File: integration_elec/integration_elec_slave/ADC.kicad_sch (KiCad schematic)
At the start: 1 part, among them U5 ADS1015IDGS

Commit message: EM - fuck it we merge et on cree deux branches
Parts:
- added R21: 2.2k, symbol Device:R_US
- added R22: 22k, Resistor_SMD:R_0805_2012Metric_Pad1.20x1.40mm_HandSolder, symbol Device:R_US
- added R23: 10k, Resistor_SMD:R_0805_2012Metric_Pad1.20x1.40mm_HandSolder, symbol Device:R_US
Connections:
- net +3V3: now also R21.1
- net GND: now also U5.1 (ADDR), R23.2
- net VO_LTF6800: now also R22.1; no longer U5.4 (AIN0)
- net I2C_SCL: now reaches U5.10 (SCL)
- net INT_ADC_OD: now reaches U5.2 (ALERT/RDY)
- net INT_ADC_OD: now also R21.2
- net I2C_SDA: now reaches U5.9 (SDA)
- new net: R22.2, R23.1, U5.4 (AIN0)
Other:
- note added: "0-10V"
- note added: "0-3V"

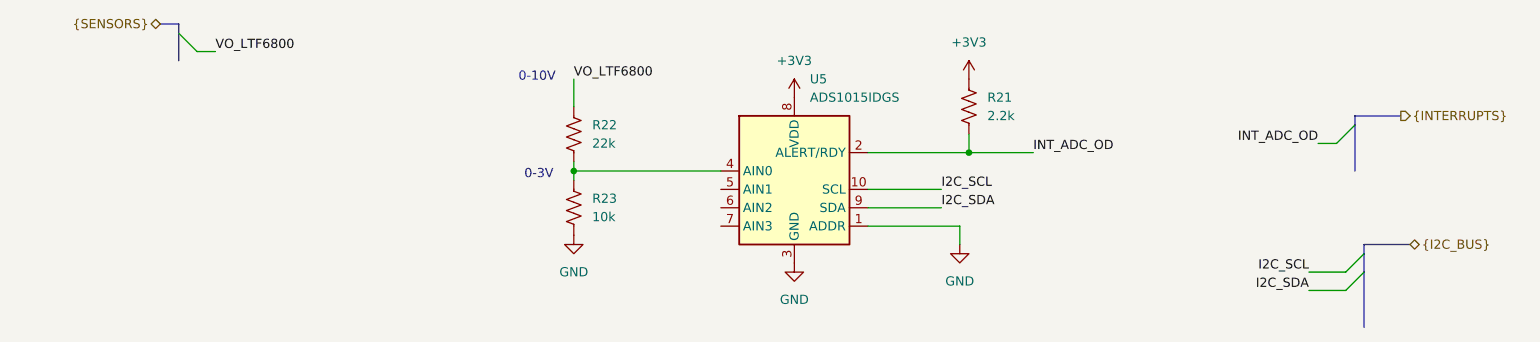
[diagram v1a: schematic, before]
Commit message: EM - Correction des bus
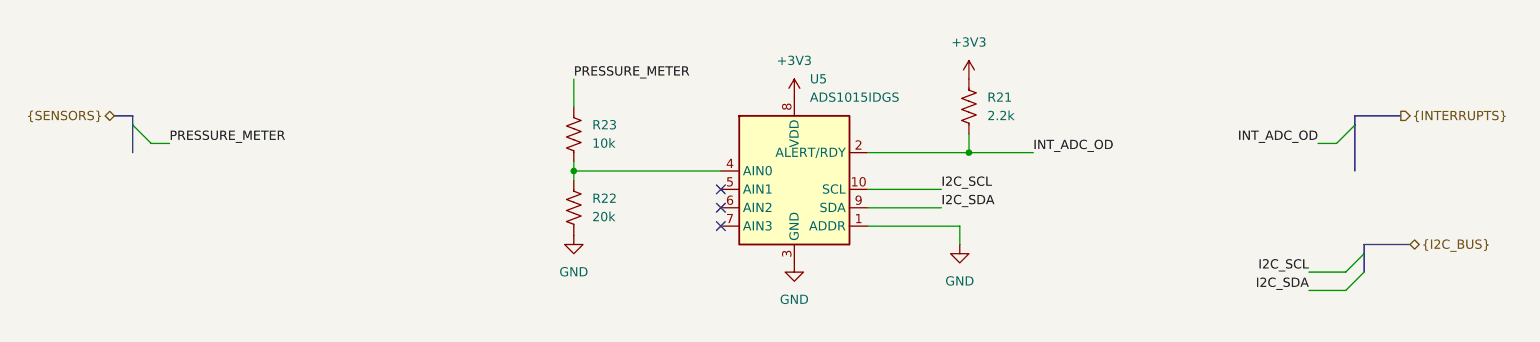
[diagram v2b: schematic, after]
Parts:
- R22: value 22k -> 20k; footprint Resistor_SMD:R_0805_2012Metric_Pad1.20x1.40mm_HandSolder -> (none)
- R23: footprint Resistor_SMD:R_0805_2012Metric_Pad1.20x1.40mm_HandSolder -> (none)
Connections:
- net GND: now also R22.2; no longer R23.2
- net VO_LTF6800: no longer names the net of R22.1
- net VO_LTF6800: now also R23.2, U5.4 (AIN0)
- new net PRESSURE_METER: R23.1
- no-connect marks 0 -> 3
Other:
- note removed: "0-10V"
- note removed: "0-3V"

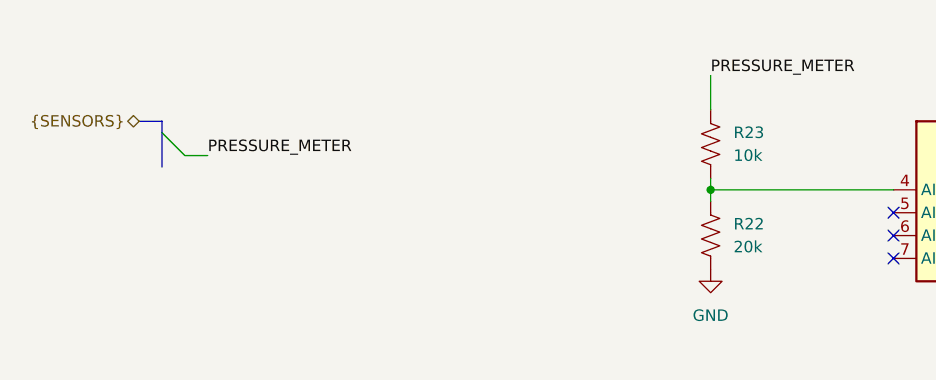
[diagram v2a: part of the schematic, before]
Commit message: EM - Fini schématique attente de review
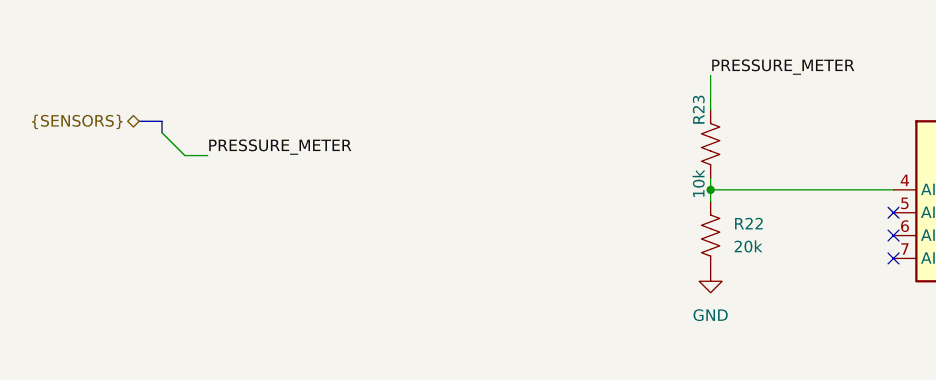
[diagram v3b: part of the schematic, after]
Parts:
- R21: footprint (none) -> Resistor_SMD:R_0805_2012Metric_Pad1.20x1.40mm_HandSolder; DigiKey (none) -> 311-2.20KCRCT-ND
- R22: footprint (none) -> Resistor_SMD:R_0805_2012Metric_Pad1.20x1.40mm_HandSolder; DigiKey (none) -> P20KDACT-ND
- R23: footprint (none) -> Resistor_SMD:R_0805_2012Metric_Pad1.20x1.40mm_HandSolder; DigiKey (none) -> 311-10.0KCRCT-ND; Manufacturer (none) -> Yageo; Manufacturer Part Number (none) -> RC0805FR-0710KL
- U5: DigiKey (none) -> 595-ADS1015IDGSR
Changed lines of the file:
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@@
-		)
-	)
-	(bus
-		(pts
-			(xy 62.23 85.09) (xy 62.23 88.9)
-		)
-		(stroke
-			(width 0)
-			(type default)
 		)
 	)
@@
 			)
 		)
-		(property "Footprint" ""
+		(property "Footprint" "Resistor_SMD:R_0805_2012Metric_Pad1.20x1.40mm_HandSolder"
 			(at 124.206 96.774 90)
 			(effects
@@
 		)
 		(property "Description" "Resistor, US symbol"
+			(at 123.19 96.52 0)
+			(effects
+				(font
+					(size 1.27 1.27)
+				)
+				(hide yes)
+			)
+		)
+		(property "DigiKey" "P20KDACT-ND"
 			(at 123.19 96.52 0)
 			(effects
@@
 				(path "/f8f45849-17b1-4cdb-b0ac-47b1208e44f3/72fa526e-6791-4af4-9337-9235f1a1456e"
 					(reference "R22")
+					(unit 1)
+				)
+			)
+		)
+	)
+	(symbol
+		(lib_id "Device:R_US")
+		(at 123.19 86.36 0)
+		(unit 1)
+		(exclude_from_sim no)
+		(in_bom yes)
+		(on_board yes)
+		(dnp no)
+		(property "Reference" "R23"
+			(at 121.92 82.55 90)
+			(effects
+				(font
+					(size 1.27 1.27)
+				)
+			)
+		)
+		(property "Value" "10k"
+			(at 121.92 90.805 90)
+			(effects
+				(font
+					(size 1.27 1.27)
+				)
+			)
+		)
+		(property "Footprint" "Resistor_SMD:R_0805_2012Metric_Pad1.20x1.40mm_HandSolder"
+			(at 124.206 86.614 90)
+			(effects
+				(font
+					(size 1.27 1.27)
+				)
+				(hide yes)
+			)
+		)
+		(property "Datasheet" "~"
+			(at 123.19 86.36 0)
+			(effects
+				(font
+					(size 1.27 1.27)
+				)
+				(hide yes)
+			)
+		)
+		(property "Description" ""
+			(at 123.19 86.36 0)
+			(effects
+				(font
+					(size 1.27 1.27)
+				)
+				(hide yes)
+			)
+		)
+		(property "DigiKey" "311-10.0KCRCT-ND"
+			(at -97.79 204.47 0)
+			(effects
+				(font
+					(size 1.27 1.27)
+				)
+				(hide yes)
+			)
+		)
+		(property "Manufacturer" "Yageo"
+			(at 34.925 135.89 0)
+			(effects
+				(font
+					(size 1.27 1.27)
+				)
+				(hide yes)
+			)
+		)
+		(property "Manufacturer Part Number" "RC0805FR-0710KL"
+			(at 34.925 135.89 0)
+			(effects
+				(font
+					(size 1.27 1.27)
+				)
+				(hide yes)
+			)
+		)
+		(pin "1"
+		)
+		(pin "2"
+		)
+		(instances
+			(project "integration_elec_slave"
+				(path "/f8f45849-17b1-4cdb-b0ac-47b1208e44f3/72fa526e-6791-4af4-9337-9235f1a1456e"
+					(reference "R23")
 					(unit 1)
 				)
@@
 	(symbol
 		(lib_id "Device:R_US")
-		(at 123.19 86.36 0)
-		(unit 1)
-		(exclude_from_sim no)
-		(in_bom yes)
-		(on_board yes)
-		(dnp no)
-		(fields_autoplaced yes)
-		(property "Reference" "R23"
-			(at 125.73 85.0899 0)
-			(effects
-				(font
-					(size 1.27 1.27)
-				)
-				(justify left)
-			)
-		)
-		(property "Value" "10k"
-			(at 125.73 87.6299 0)
-			(effects
-				(font
-					(size 1.27 1.27)
-				)
-				(justify left)
-			)
-		)
-		(property "Footprint" ""
-			(at 124.206 86.614 90)
-			(effects
-				(font
-					(size 1.27 1.27)
-				)
-				(hide yes)
-			)
-		)
-		(property "Datasheet" "~"
-			(at 123.19 86.36 0)
-			(effects
-				(font
-					(size 1.27 1.27)
-				)
-				(hide yes)
-			)
-		)
-		(property "Description" "Resistor, US symbol"
-			(at 123.19 86.36 0)
-			(effects
-				(font
-					(size 1.27 1.27)
-				)
-				(hide yes)
-			)
-		)
-		(pin "1"
-		)
-		(pin "2"
-		)
-		(instances
-			(project ""
-				(path "/f8f45849-17b1-4cdb-b0ac-47b1208e44f3/72fa526e-6791-4af4-9337-9235f1a1456e"
-					(reference "R23")
-					(unit 1)
-				)
-			)
-		)
-	)
-	(symbol
-		(lib_id "Device:R_US")
 		(at 177.8 82.55 0)
 		(unit 1)
@@
 			)
 		)
-		(property "Footprint" ""
+		(property "Footprint" "Resistor_SMD:R_0805_2012Metric_Pad1.20x1.40mm_HandSolder"
 			(at 178.816 82.804 90)
 			(effects
@@
 		)
 		(property "Description" "Resistor, US symbol"
+			(at 177.8 82.55 0)
+			(effects
+				(font
+					(size 1.27 1.27)
+				)
+				(hide yes)
+			)
+		)
+		(property "DigiKey" "311-2.20KCRCT-ND"
 			(at 177.8 82.55 0)
 			(effects
@@
 			(at 153.67 93.98 0)
 			(effects
+				(font
+					(size 1.27 1.27)
+				)
+				(hide yes)
+			)
+		)
+		(property "DigiKey" "595-ADS1015IDGSR "
+			(at 153.67 93.98 0)
+			(effects

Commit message: EM - Review pas mal finale
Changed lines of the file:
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@@
 		)
 		(property "Value" "10k"
-			(at 121.92 90.805 90)
+			(at 125.476 86.36 90)
 			(effects
 				(font
